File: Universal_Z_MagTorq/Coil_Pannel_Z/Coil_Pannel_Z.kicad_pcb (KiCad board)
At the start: 6 copper layers, 194.1 x 144 mm, 8 parts, among them J1 2053380002

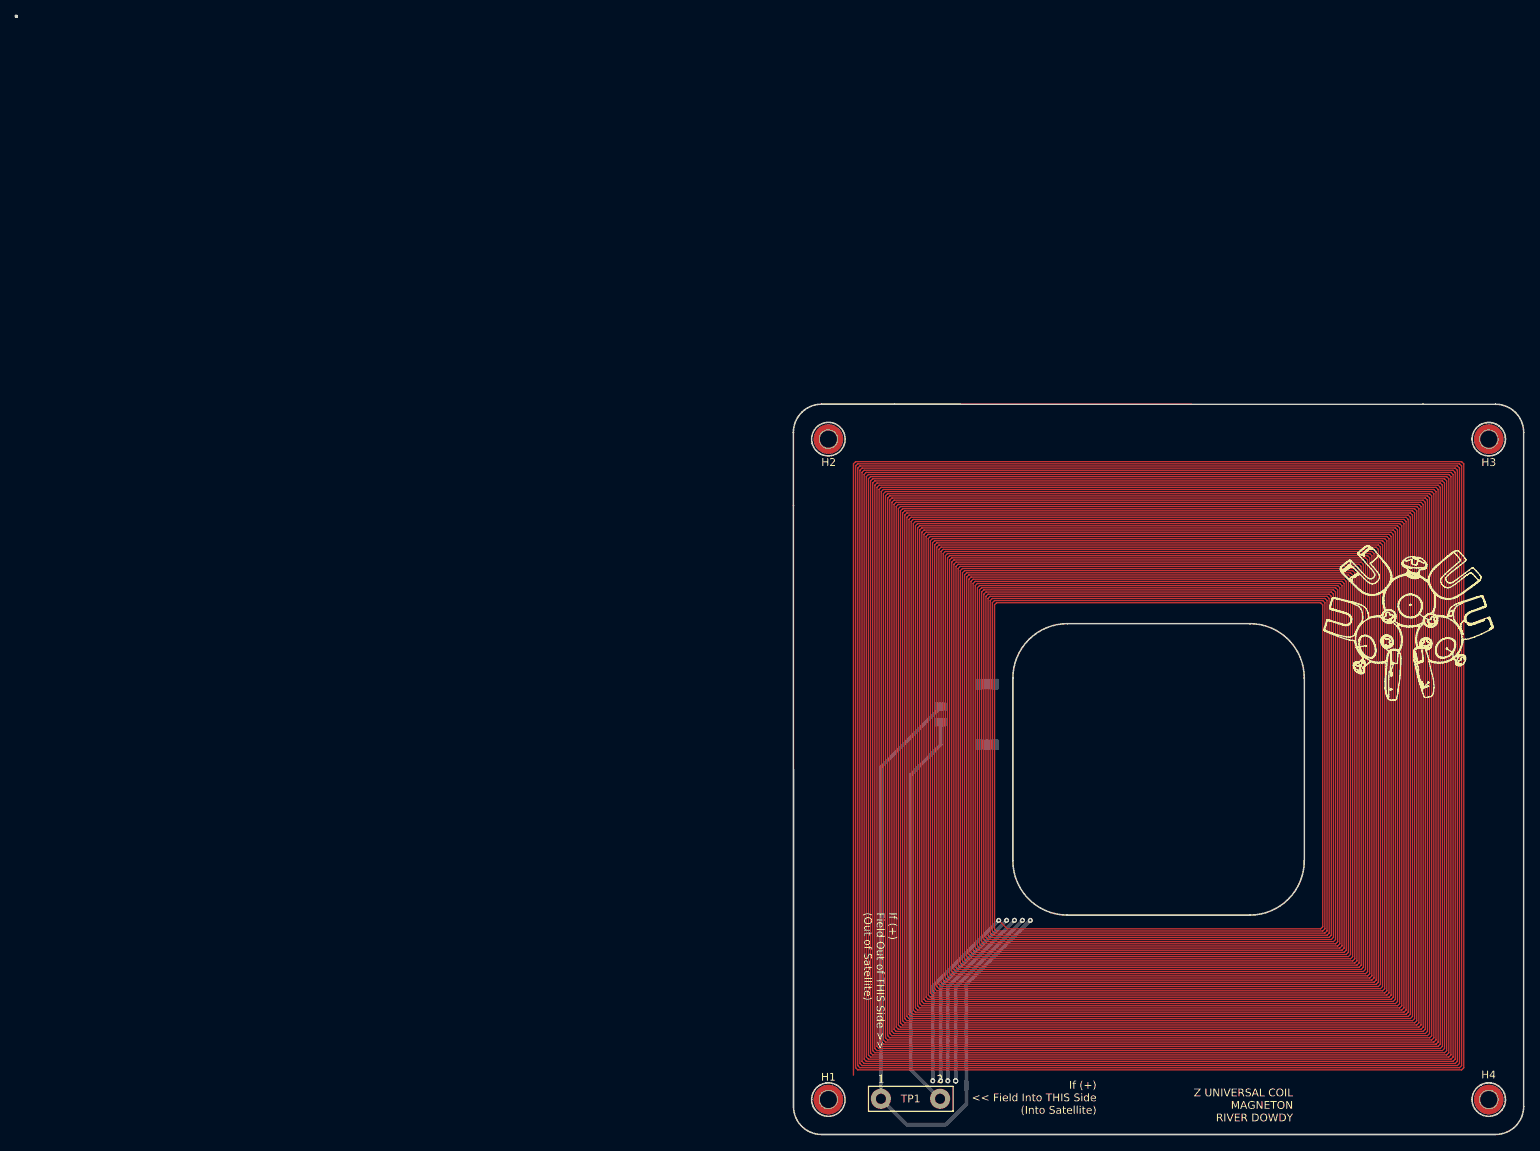
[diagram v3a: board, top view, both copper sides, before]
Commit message: updated hole sizing
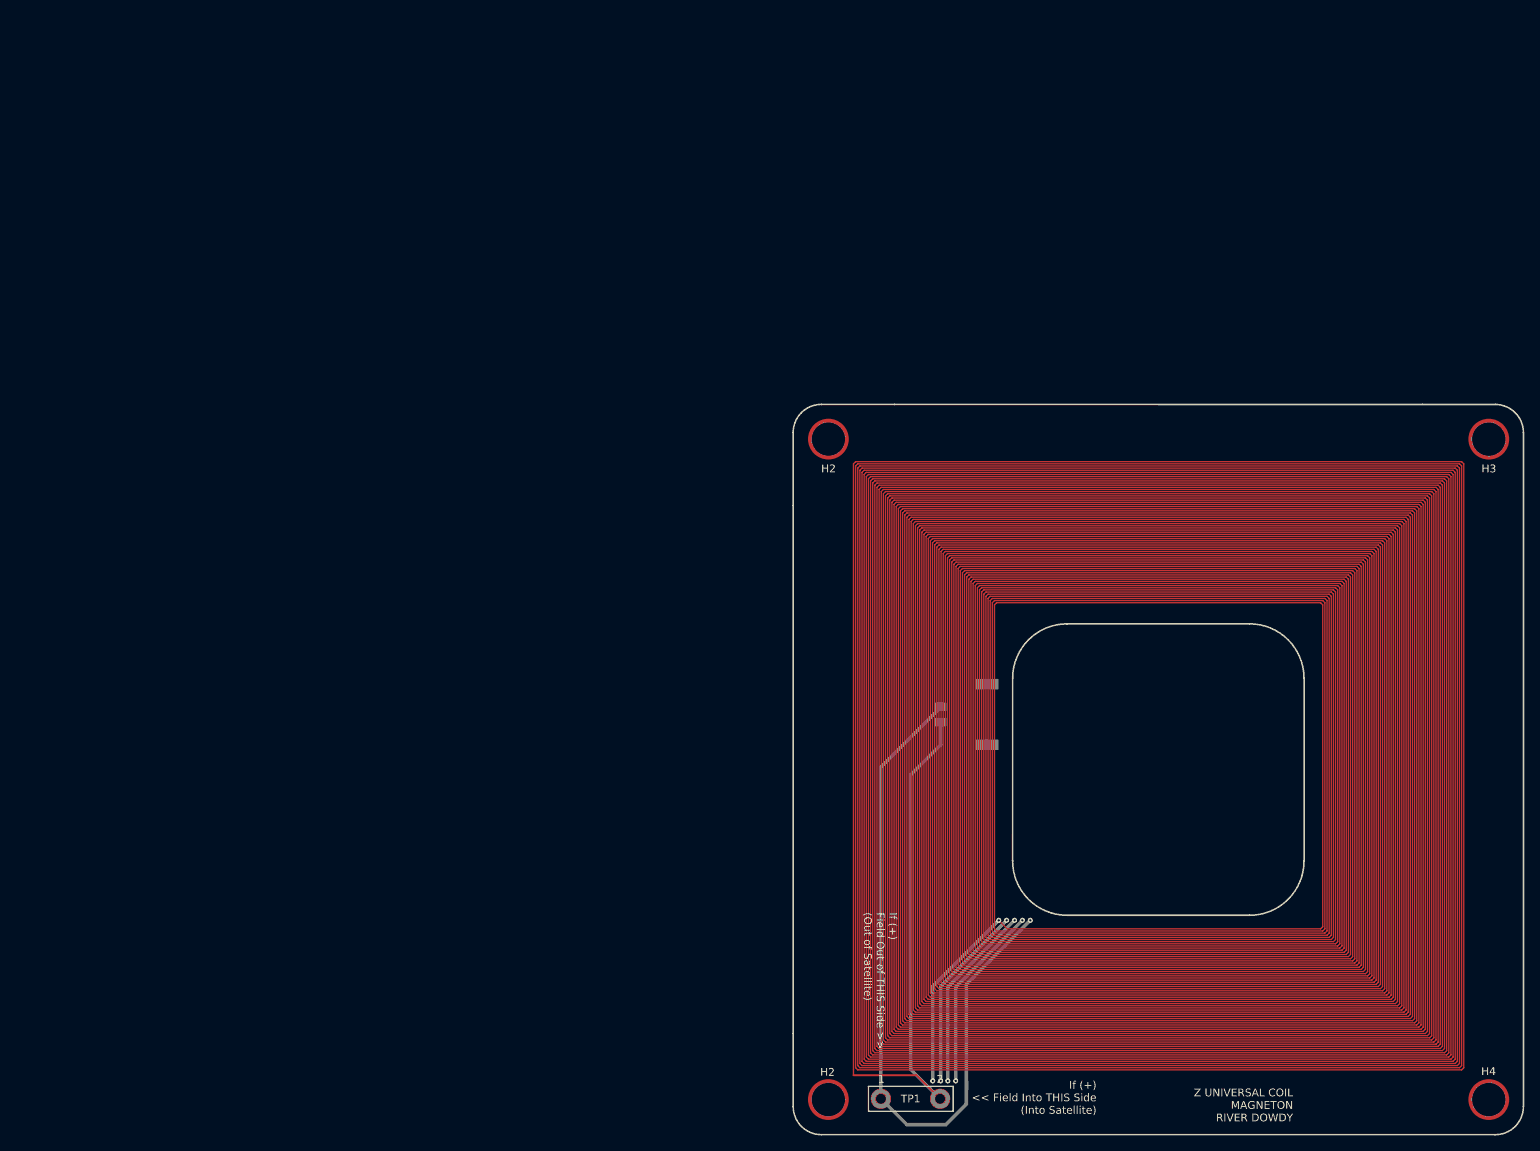
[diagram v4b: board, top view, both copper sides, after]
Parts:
- removed H1: ~, MountingHole:MountingHole_2.2mm_M2_DIN965_Pad_TopBottom
- added ? (x2): , , F.Cu at (104.6, 138.9)
- REF**: moved to B.Cu
- moved REF** 23.5 mm to (191.8, 88.0), turned to 180 degrees
- turned H4 to 0 degrees
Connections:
- H3 pad 1: unconnected-(H3-Pad1) -> (no net)
- H4 pad 1: unconnected-(H4-Pad1)_2 -> (no net)
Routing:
- net COIL_2: track 80748.7 -> 80761.1 mm, vias 10 -> 9
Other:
- board size 194.1 x 144 mm -> 94 x 94 mm
- board text added: "H2"

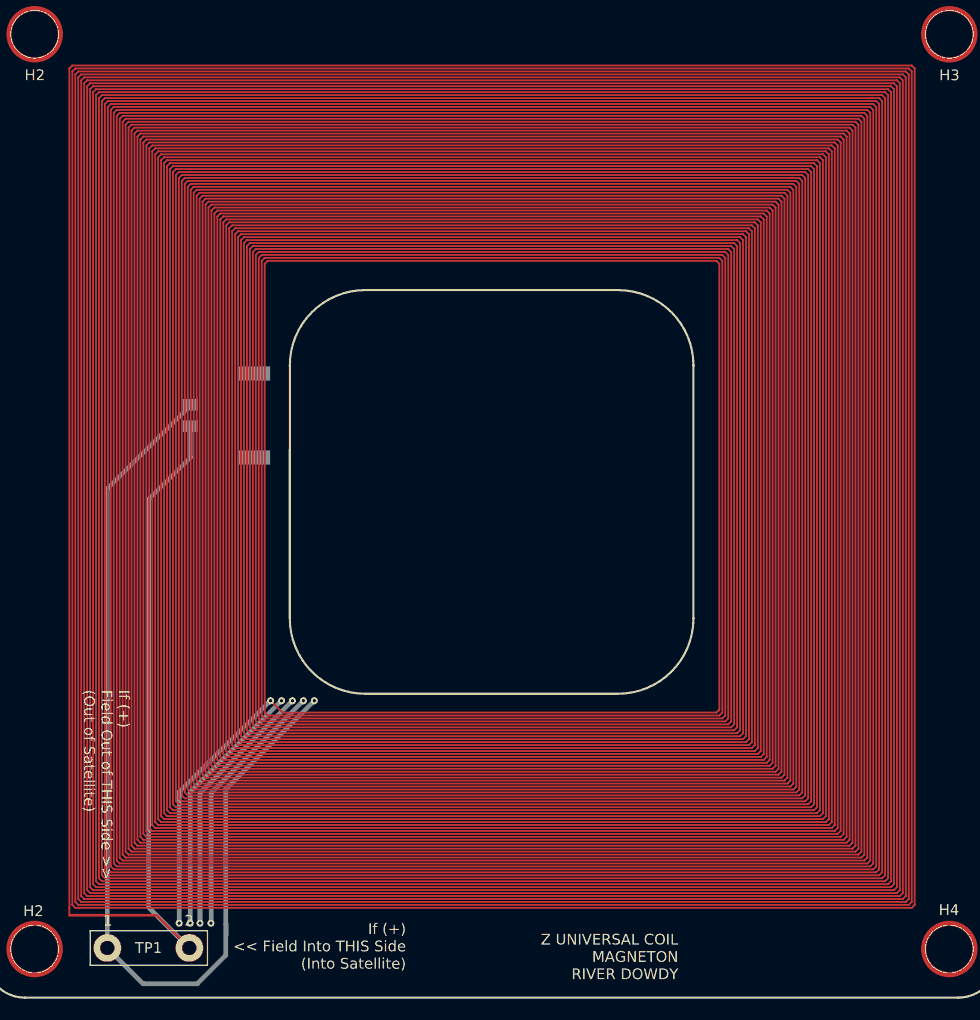
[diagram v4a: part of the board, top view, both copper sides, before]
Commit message: Updated correct trace width and spacing
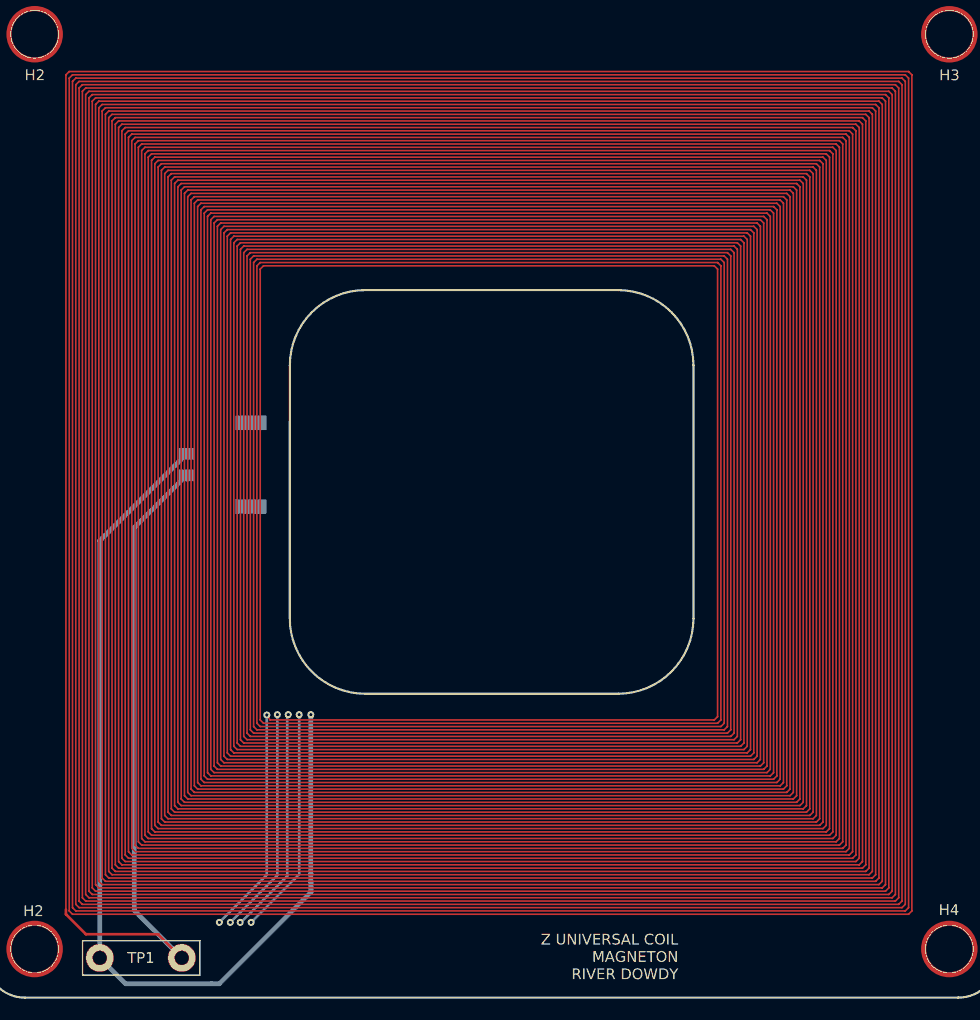
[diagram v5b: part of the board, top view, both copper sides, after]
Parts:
- moved NT1 8.83 mm to (130.3, 133.2), turned to 90 degrees
- moved J1 4.59 mm to (118.8, 92.9)
- moved TP1 1.16 mm to (114.5, 140.3)
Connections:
- NT1 pad 1: COIL_2 -> COIL_1
- NT1 pad 2: COIL_1 -> COIL_2
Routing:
- net COIL_2: track 80761.1 -> 72485.1 mm
- net COIL_1: track 69.0 -> 74.3 mm
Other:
- board text removed: "1"
- board text removed: "2"
- board text removed: "<< If (+) Field Into This Side (Out of Satellite)"
- board text removed: "<< If (+) Field Out of This Side (Into Satellite)"
- board text removed: "If (+) << Field Into THIS Side (Into Satellite)"
- board text removed: "If (+) << Field Into THIS Side (Out of Satellite)"
- board text removed: "If (+) Field Out of THIS Side >> (Into Satellite)"
- board text removed: "If (+) Field Out of THIS Side >> (Out of Satellite)"
